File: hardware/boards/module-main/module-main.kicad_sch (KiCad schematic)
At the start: 2 parts, among them J2 2x10 2.54mm pin header, J3 Neutrik NE8FAV

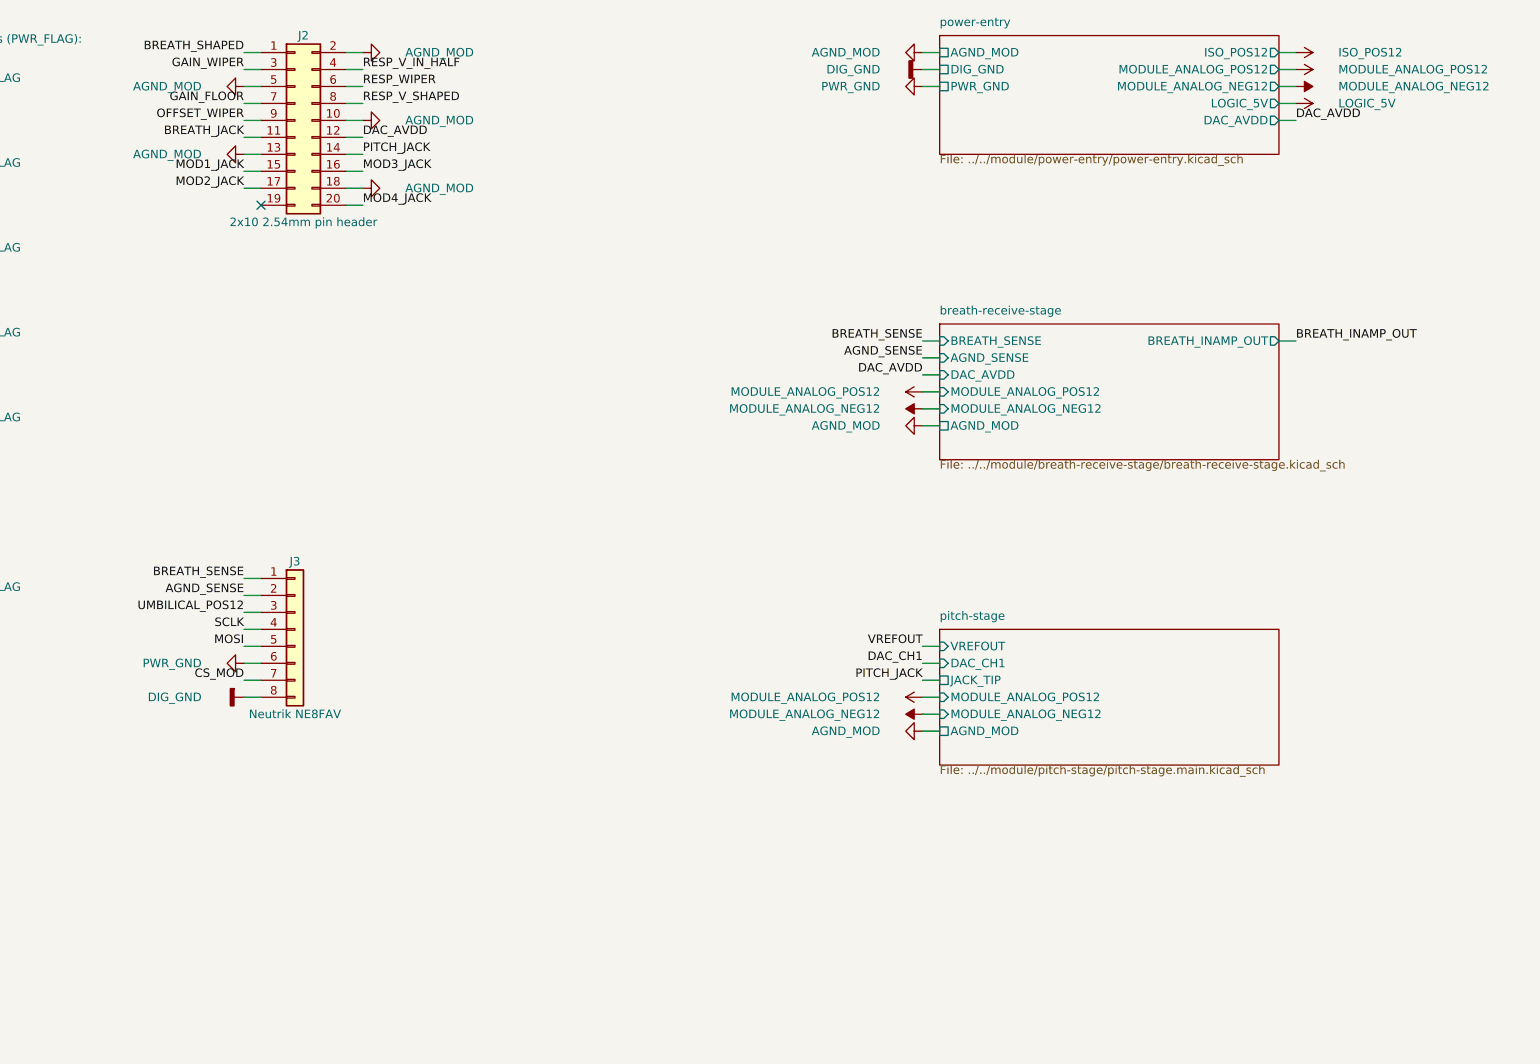
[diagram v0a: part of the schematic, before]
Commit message: Module: a third board, the iso board, for U-ISO and its filter (owner: "3 boards for module is correct")
The main board could not be routed cleanly with U-ISO's 25 mm body, its pins and
its isolation gap in the middle of the DAC corner (re-placing that corner first left
35 connections, worse than the 20 before). So the instrument's isolated supply
moves to a board of its own, behind the main board:

- CAD: config/module.yaml iso_board (top edge, three spacers, under_h) and
  b2b_iso; U-ISO and its filter now on the iso board's rear face. module.scad
  derives the outline (side edges, above the NE8FAV's tails, a notch for
  J-PWR-EURO), the gap (the stock 8 mm spacer, uncut) and J-B2B-ISO's pin
  length, and DRCs the iso board: parts inside, clear of each other, the gap,
  the main board's tall rear parts, the ribbon fold, trimmer access, depth.
  iso-board.dxf and pcb-geometry lines for module-iso; the boards figure draws
  all three. Bulk-cap envelopes move above the iso board.
- Sheets: power-entry is a parent placing two pages, main and iso, exported
  netlist unchanged but for order. module-main's root takes J-B2B-ISO (J5);
  hardware/boards/module-iso is the new board's project.
- BOM: J-B2B-ISO (TSW-105-09-G-D, candidate), PCB-MODULE-ISO,
  MECH-STANDOFF-ISO; MECH-STANDOFF-SCREW-MOD 6 -> 12.
- Tools: J-B2B-ISO in kicad.py's through check and pcb_module's fixed pads and
  b2b check (now a list of headers); complete() ignores a THT pad's inner
  layer on a two-layer board.
- module-iso laid out and routed, two layers: pcb.py check passes but for the
  B2B mate, which waits for module-main's new layout.

Co-Authored-By: Claude Opus 5.5 <noreply@anthropic.com>
Claude-Session: https://claude.ai/code/session_01LmB4muFXnoLprWX4JzuJ5A
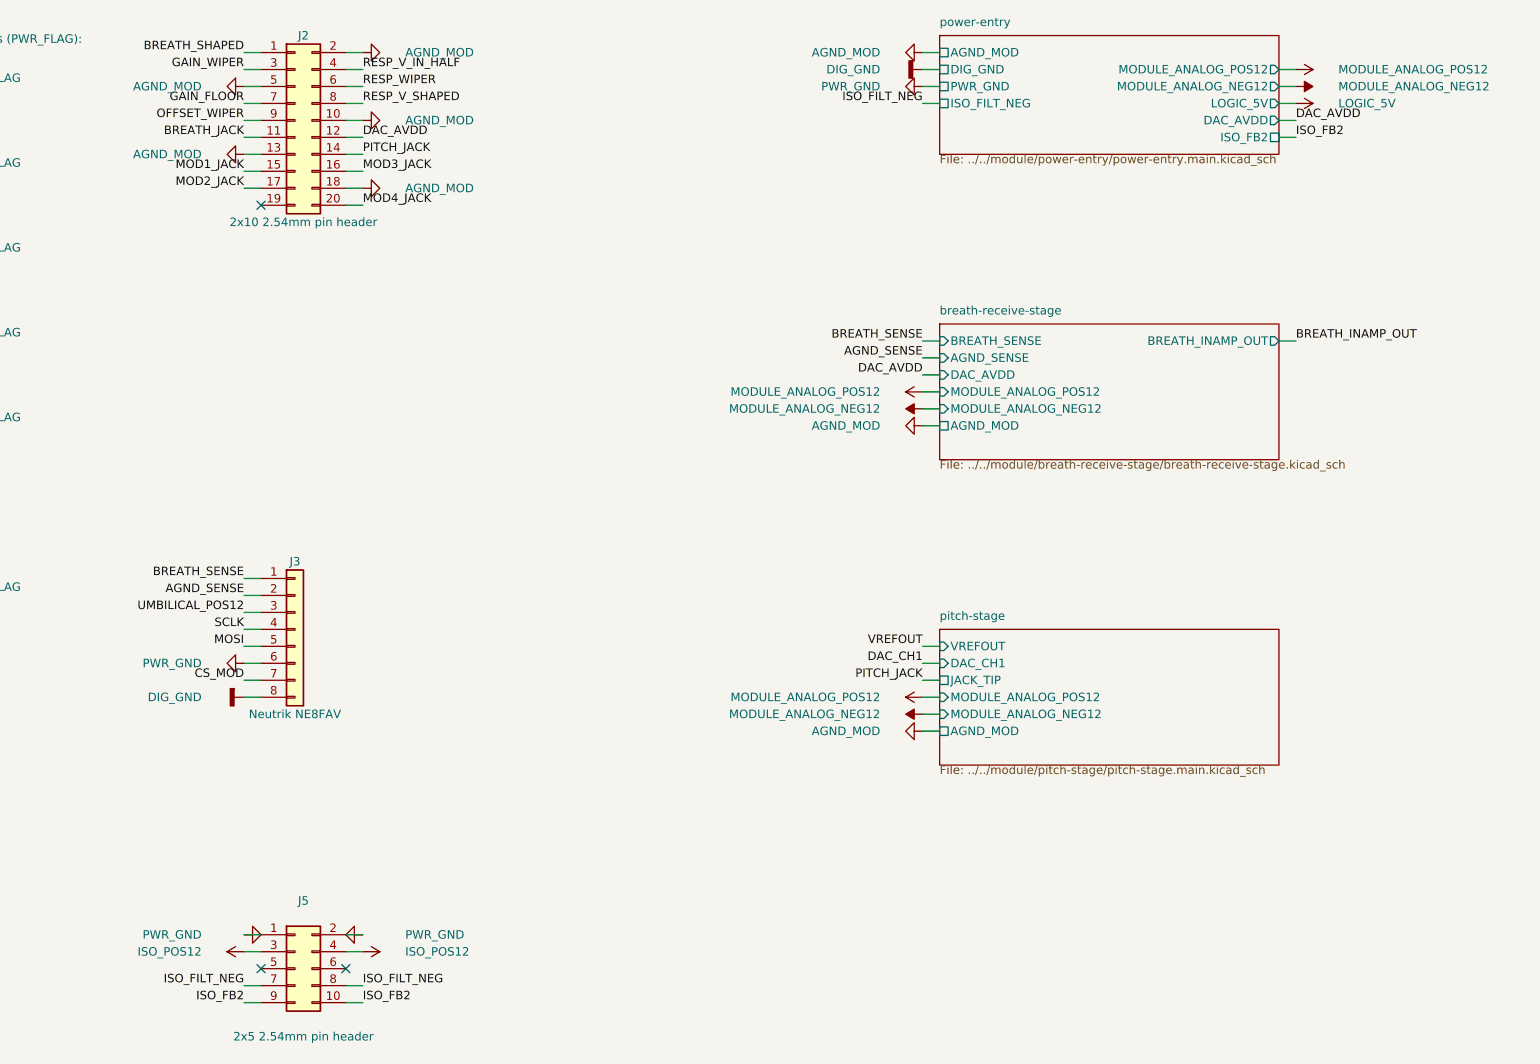
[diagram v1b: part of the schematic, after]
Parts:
- added J5: 2x5 2.54mm pin header, Connector_PinHeader_2.54mm:PinHeader_2x05_P2.54mm_Vertical, symbol Connector_Generic:Conn_02x05_Odd_Even
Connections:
- net ISO_POS12: now also J5.3 (Pin_3), J5.4 (Pin_4)
- net PWR_GND: now also J5.1 (Pin_1), J5.2 (Pin_2)
- new net ISO_FB2: J5.10 (Pin_10), J5.9 (Pin_9)
- new net ISO_FILT_NEG: J5.7 (Pin_7), J5.8 (Pin_8)
- no-connect marks 1 -> 3
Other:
- sheet power-entry: file ../../module/power-entry/power-entry.kicad_sch -> ../../module/power-entry/power-entry.main.kicad_sch
- sheet power-entry ports: added ISO_FB2, ISO_FILT_NEG; removed ISO_POS12
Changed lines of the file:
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@@
     (comment 1 "SOURCE for the board - edit in KiCad 9. board-netlist.yaml is exported from it: python3 tools/kicad.py export hardware/boards/module-main")
     (comment 2 "Part facts ride on each symbol: Row (BOM row), Pins + Pins_source (pin map and its datasheet), Note")
-    (comment 3 "ADR 0019, ADR 0023 - the module circuits' pages placed once each; J-B2B-MOD joins the two boards")
+    (comment 3 "ADR 0019, ADR 0023 - the module circuits' pages placed once each; J-B2B-MOD joins the jack board, J-B2B-ISO the iso board")
     (comment 4 "SOURCE - edit in KiCad 9; tools/kicad.py exports board-netlist.yaml")
   )
@@
   (wire (pts (xy 381.0 53.34) (xy 383.54 53.34)) (stroke (width 0) (type default)))
   (label "UMBILICAL_POS12" (at 383.54 53.34 0) (fields_autoplaced) (effects (font (size 1.27 1.27)) (justify left bottom)))
-  (wire (pts (xy 254.0 53.34) (xy 256.54 53.34)) (stroke (width 0) (type default)))
-  (symbol (lib_id "power:+12V") (at 256.54 53.34 270) (unit 1)
-    (in_bom yes) (on_board yes) (dnp no)
-    (property "Reference" "#PWR26" (at 252.73 53.34 0) (effects (font (size 1.27 1.27)) hide))
-    (property "Value" "ISO_POS12" (at 262.89 53.34 270) (effects (font (size 1.27 1.27)) (justify right)))
-    (property "Footprint" "" (at 256.54 53.34 0) (effects (font (size 1.27 1.27)) hide))
-    (property "Datasheet" "" (at 256.54 53.34 0) (effects (font (size 1.27 1.27)) hide))
-    (pin "1")
-    (instances (project "module-main" (path "/fc77e9f9-9171-5c83-92ae-8cafe880764e" (reference "#PWR26") (unit 1))))
-  )
   (wire (pts (xy 330.2 53.34) (xy 327.66 53.34)) (stroke (width 0) (type default)))
   (symbol (lib_id "power:+12V") (at 327.66 53.34 90) (unit 1)
@@
     (stroke (width 0.1524) (type solid)) (fill (color 0 0 0 0.0000))
     (property "Sheetname" "power-entry" (at 203.2 49.53 0) (effects (font (size 1.27 1.27)) (justify left bottom)))
-    (property "Sheetfile" "../../module/power-entry/power-entry.kicad_sch" (at 203.2 68.58 0) (effects (font (size 1.27 1.27)) (justify left top)))
+    (property "Sheetfile" "../../module/power-entry/power-entry.main.kicad_sch" (at 203.2 68.58 0) (effects (font (size 1.27 1.27)) (justify left top)))
     (pin "AGND_MOD" passive (at 203.2 53.34 180) (effects (font (size 1.27 1.27)) (justify left)))
     (pin "DIG_GND" passive (at 203.2 55.88 180) (effects (font (size 1.27 1.27)) (justify left)))
     (pin "PWR_GND" passive (at 203.2 58.42 180) (effects (font (size 1.27 1.27)) (justify left)))
-    (pin "ISO_POS12" output (at 254.0 53.34 0) (effects (font (size 1.27 1.27)) (justify right)))
     (pin "MODULE_ANALOG_POS12" output (at 254.0 55.88 0) (effects (font (size 1.27 1.27)) (justify right)))
     (pin "MODULE_ANALOG_NEG12" output (at 254.0 58.42 0) (effects (font (size 1.27 1.27)) (justify right)))
     (pin "LOGIC_5V" output (at 254.0 60.96 0) (effects (font (size 1.27 1.27)) (justify right)))
     (pin "DAC_AVDD" output (at 254.0 63.5 0) (effects (font (size 1.27 1.27)) (justify right)))
+    (pin "ISO_FB2" passive (at 254.0 66.04 0) (effects (font (size 1.27 1.27)) (justify right)))
+    (pin "ISO_FILT_NEG" passive (at 203.2 60.96 180) (effects (font (size 1.27 1.27)) (justify left)))
     (instances (project "module-main" (path "/fc77e9f9-9171-5c83-92ae-8cafe880764e" (page "2"))))
   )
@@
     (instances (project "module-main" (path "/fc77e9f9-9171-5c83-92ae-8cafe880764e" (page "11"))))
   )
+  (wire (pts (xy 254.0 66.04) (xy 256.54 66.04)) (stroke (width 0) (type default)))
+  (label "ISO_FB2" (at 256.54 66.04 0) (fields_autoplaced) (effects (font (size 1.27 1.27)) (justify left bottom)))
+  (wire (pts (xy 203.2 60.96) (xy 200.66 60.96)) (stroke (width 0) (type default)))
+  (label "ISO_FILT_NEG" (at 200.66 60.96 180) (fields_autoplaced) (effects (font (size 1.27 1.27)) (justify right bottom)))
+  (symbol (lib_id "Connector_Generic:Conn_02x05_Odd_Even") (at 106.68 190.5 0) (unit 1)
+    (in_bom yes) (on_board yes) (dnp no)
+    (property "Reference" "J5" (at 107.95 180.34 0) (effects (font (size 1.27 1.27))))
+    (property "Value" "2x5 2.54mm pin header" (at 107.95 200.66 0) (effects (font (size 1.27 1.27))))
+    (property "Footprint" "Connector_PinHeader_2.54mm:PinHeader_2x05_P2.54mm_Vertical" (at 106.68 190.5 0) (effects (font (size 1.27 1.27)) hide))
+    (property "Datasheet" "" (at 106.68 190.5 0) (effects (font (size 1.27 1.27)) hide))
+    (property "Row" "J-B2B-ISO" (at 106.68 190.5 0) (effects (font (size 1.27 1.27)) hide))
+    (property "Pins" "1=1 2=2 3=3 4=4 5=5 6=6 7=7 8=8 9=9 10=10" (at 106.68 190.5 0) (effects (font (size 1.27 1.27)) hide))
+    (property "Note" "Soldered through the module main board and the iso board, no mated contact (ADR 0023, amended 2026-10-03). Its pin k is the same conductor on both boards; tools/kicad.py check holds the two sheets to that. Pairs: 1-2 PWR_GND, 3-4 ISO_POS12, 5-6 unconnected (the isolation gap), 7-8 ISO_FILT_NEG, 9-10 ISO_FB2. hardware/boards/module-iso/README.md" (at 106.68 190.5 0) (effects (font (size 1.27 1.27)) hide))
+    (property "Pins_source" "header position n on pin n, odd/even across the two rows as a 2x5 header numbers them" (at 106.68 190.5 0) (effects (font (size 1.27 1.27)) hide))
+    (property "Manufacturer" "Samtec" (at 106.68 190.5 0) (effects (font (size 1.27 1.27)) hide))
+    (property "MPN" "TSW-105-09-G-D" (at 106.68 190.5 0) (effects (font (size 1.27 1.27)) hide))
+    (property "LCSC" "" (at 106.68 190.5 0) (effects (font (size 1.27 1.27)) hide))
+    (property "Assembly" "hand" (at 106.68 190.5 0) (effects (font (size 1.27 1.27)) hide))
+    (pin "1")
+    (pin "2")
+    (pin "3")
+    (pin "4")
+    (pin "5")
+    (pin "6")
+    (pin "7")
+    (pin "8")
+    (pin "9")
+    (pin "10")
+    (instances (project "module-main" (path "/fc77e9f9-9171-5c83-92ae-8cafe880764e" (reference "J5") (unit 1))))
+  )
+  (wire (pts (xy 101.60 185.42) (xy 99.06 185.42)) (stroke (width 0) (type default)))
+  (symbol (lib_id "power:GND") (at 99.06 185.42 90) (unit 1)
+    (in_bom yes) (on_board yes) (dnp no)
+    (property "Reference" "#PWR901" (at 99.06 185.42 0) (effects (font (size 1.27 1.27)) hide))
+    (property "Value" "PWR_GND" (at 92.71 185.42 90) (effects (font (size 1.27 1.27)) (justify left)))
+    (property "Footprint" "" (at 99.06 185.42 0) (effects (font (size 1.27 1.27)) hide))
+    (property "Datasheet" "" (at 99.06 185.42 0) (effects (font (size 1.27 1.27)) hide))
+    (pin "1")
+    (instances (project "module-main" (path "/fc77e9f9-9171-5c83-92ae-8cafe880764e" (reference "#PWR901") (unit 1))))
+  )
+  (wire (pts (xy 114.30 185.42) (xy 116.84 185.42)) (stroke (width 0) (type default)))
+  (symbol (lib_id "power:GND") (at 116.84 185.42 270) (unit 1)
+    (in_bom yes) (on_board yes) (dnp no)
+    (property "Reference" "#PWR902" (at 116.84 185.42 0) (effects (font (size 1.27 1.27)) hide))
+    (property "Value" "PWR_GND" (at 123.19 185.42 270) (effects (font (size 1.27 1.27)) (justify right)))
+    (property "Footprint" "" (at 116.84 185.42 0) (effects (font (size 1.27 1.27)) hide))
+    (property "Datasheet" "" (at 116.84 185.42 0) (effects (font (size 1.27 1.27)) hide))
+    (pin "1")
+    (instances (project "module-main" (path "/fc77e9f9-9171-5c83-92ae-8cafe880764e" (reference "#PWR902") (unit 1))))
+  )
+  (wire (pts (xy 101.60 187.96) (xy 99.06 187.96)) (stroke (width 0) (type default)))
+  (symbol (lib_id "power:+12V") (at 99.06 187.96 90) (unit 1)
+    (in_bom yes) (on_board yes) (dnp no)
+    (property "Reference" "#PWR903" (at 99.06 187.96 0) (effects (font (size 1.27 1.27)) hide))
+    (property "Value" "ISO_POS12" (at 92.71 187.96 90) (effects (font (size 1.27 1.27)) (justify left)))
+    (property "Footprint" "" (at 99.06 187.96 0) (effects (font (size 1.27 1.27)) hide))
+    (property "Datasheet" "" (at 99.06 187.96 0) (effects (font (size 1.27 1.27)) hide))
+    (pin "1")
+    (instances (project "module-main" (path "/fc77e9f9-9171-5c83-92ae-8cafe880764e" (reference "#PWR903") (unit 1))))
+  )
+  (wire (pts (xy 114.30 187.96) (xy 116.84 187.96)) (stroke (width 0) (type default)))
+  (symbol (lib_id "power:+12V") (at 116.84 187.96 270) (unit 1)
+    (in_bom yes) (on_board yes) (dnp no)
+    (property "Reference" "#PWR904" (at 116.84 187.96 0) (effects (font (size 1.27 1.27)) hide))
+    (property "Value" "ISO_POS12" (at 123.19 187.96 270) (effects (font (size 1.27 1.27)) (justify right)))
+    (property "Footprint" "" (at 116.84 187.96 0) (effects (font (size 1.27 1.27)) hide))
+    (property "Datasheet" "" (at 116.84 187.96 0) (effects (font (size 1.27 1.27)) hide))
+    (pin "1")
+    (instances (project "module-main" (path "/fc77e9f9-9171-5c83-92ae-8cafe880764e" (reference "#PWR904") (unit 1))))
+  )
+  (no_connect (at 101.60 190.50))
+  (no_connect (at 114.30 190.50))
+  (wire (pts (xy 101.60 193.04) (xy 99.06 193.04)) (stroke (width 0) (type default)))
+  (label "ISO_FILT_NEG" (at 99.06 193.04 180) (fields_autoplaced) (effects (font (size 1.27 1.27)) (justify right bottom)))
+  (wire (pts (xy 114.30 193.04) (xy 116.84 193.04)) (stroke (width 0) (type default)))
+  (label "ISO_FILT_NEG" (at 116.84 193.04 0) (fields_autoplaced) (effects (font (size 1.27 1.27)) (justify left bottom)))
+  (wire (pts (xy 101.60 195.58) (xy 99.06 195.58)) (stroke (width 0) (type default)))
+  (label "ISO_FB2" (at 99.06 195.58 180) (fields_autoplaced) (effects (font (size 1.27 1.27)) (justify right bottom)))
+  (wire (pts (xy 114.30 195.58) (xy 116.84 195.58)) (stroke (width 0) (type default)))
+  (label "ISO_FB2" (at 116.84 195.58 0) (fields_autoplaced) (effects (font (size 1.27 1.27)) (justify left bottom)))
   (sheet_instances (path "/" (page "1")))
 )

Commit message: #32: checkpoint — switchable breath band-limit, 1.5 kHz ADC filter, breath LED
Receive stage: C_diff switched by U-BW-SW (TMUX6112) from SW-BREATH-BW
(NKK M2024, left 500 Hz / centre 1.5 kHz / right WIDE): 680 pF fixed,
3.9 nF and 10 nF switched; C_cm 68 pF matched pair. C-OUT-BREATH 10 nF C0G.
C-AA-ADC 18 nF (1.47 kHz), sample rate kept at 4 kHz. Breath LED driver on
U-REF-BUF B. Sheets, BOM fragments, datasheets (TMUX6112, MMBT3904), sims,
ADR 0003/0004 amendments, pages. Sims still being re-run.

Gate-Red: sims stale while re-running (breath-receive-stage, breath-output-stage, interfaces/system, pitch-stage); breath-sense-link/sim pg_gain_max < 1e-3 fails in every mode and power-entry/sim led-pwm breath_mv fails at 2 kHz - both consequences of #32 left for the owner, not loosened; breath-receive-stage cmrr-wide fails 58.5 dB above ~7.4 kHz (owner); kicad: module-main and main-board .kicad_pcb parity broken by the new/changed parts (re-placement is the module re-layout's; pcb not touched), plus module-main's pre-existing routing failures

Co-Authored-By: Claude Opus 5.5 <noreply@anthropic.com>
Claude-Session: https://claude.ai/code/session_01LmB4muFXnoLprWX4JzuJ5A
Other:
- sheet breath-output-stage ports: added BREATH_OUT; removed none
- sheet breath-receive-stage ports: added BREATH_OUT; removed none
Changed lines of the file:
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@@
     (pin "MODULE_ANALOG_NEG12" input (at 203.2 106.68 180) (effects (font (size 1.27 1.27)) (justify left)))
     (pin "AGND_MOD" passive (at 203.2 109.22 180) (effects (font (size 1.27 1.27)) (justify left)))
+    (pin "BREATH_OUT" input (at 203.2 111.76 180) (effects (font (size 1.27 1.27)) (justify left)))
     (pin "BREATH_INAMP_OUT" output (at 254.0 96.52 0) (effects (font (size 1.27 1.27)) (justify right)))
     (instances (project "module-main" (path "/fc77e9f9-9171-5c83-92ae-8cafe880764e" (page "6"))))
@@
     (pin "JACK_TIP" passive (at 457.2 114.3 180) (effects (font (size 1.27 1.27)) (justify left)))
     (pin "AGND_MOD" passive (at 457.2 116.84 180) (effects (font (size 1.27 1.27)) (justify left)))
+    (pin "BREATH_OUT" output (at 457.2 119.38 180) (effects (font (size 1.27 1.27)) (justify left)))
     (instances (project "module-main" (path "/fc77e9f9-9171-5c83-92ae-8cafe880764e" (page "7"))))
   )
@@
   (wire (pts (xy 114.30 195.58) (xy 116.84 195.58)) (stroke (width 0) (type default)))
   (label "ISO_FB2" (at 116.84 195.58 0) (fields_autoplaced) (effects (font (size 1.27 1.27)) (justify left bottom)))
+  (wire (pts (xy 203.2 111.76) (xy 200.66 111.76)) (stroke (width 0) (type default)))
+  (label "BREATH_OUT" (at 200.66 111.76 180) (fields_autoplaced) (effects (font (size 1.27 1.27)) (justify right bottom)))
+  (wire (pts (xy 457.2 119.38) (xy 454.66 119.38)) (stroke (width 0) (type default)))
+  (label "BREATH_OUT" (at 454.66 119.38 180) (fields_autoplaced) (effects (font (size 1.27 1.27)) (justify right bottom)))
   (sheet_instances (path "/" (page "1")))
 )
